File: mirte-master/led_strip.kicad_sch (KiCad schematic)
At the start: 2 parts, among them J24 led_strip

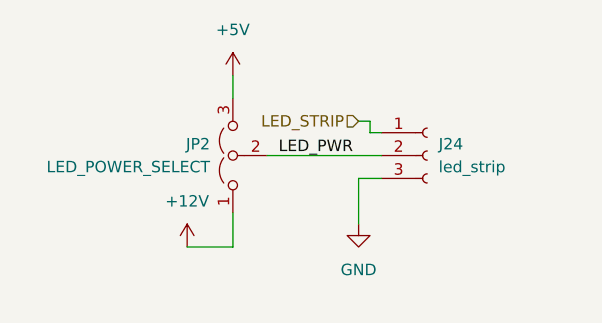
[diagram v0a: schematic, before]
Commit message: add kerco/elcos
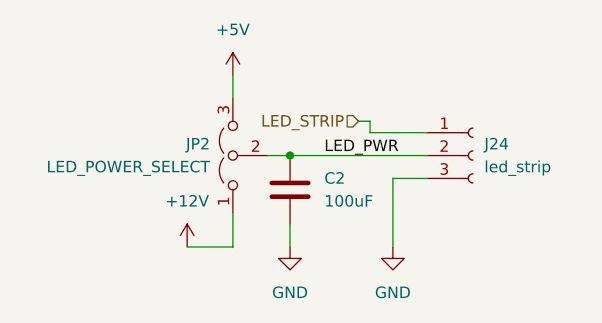
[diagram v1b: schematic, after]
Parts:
- added C2: 100uF, Capacitor_SMD:C_0805_2012Metric, symbol Device:C
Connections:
- net GND: now also C2.2
- net LED_PWR: now also C2.1
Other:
- moved on the sheet: J24
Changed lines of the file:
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@@
 (kicad_sch (version 20230121) (generator eeschema)
   (paper "A4")
-  (wire (pts (xy 113.03 73.66) (xy 110.49 73.66))
+  (junction (at 102.87 71.12) (diameter 0) (color 0 0 0 0)
+  )
+  (wire (pts (xy 118.11 73.66) (xy 114.3 73.66))
     (stroke (width 0) (type default))
   )
@@
     (stroke (width 0) (type default))
   )
-  (wire (pts (xy 111.76 68.58) (xy 113.03 68.58))
-    (stroke (width 0) (type default))
-  )
-  (wire (pts (xy 110.49 73.66) (xy 110.49 78.74))
+  (wire (pts (xy 111.76 68.58) (xy 118.11 68.58))
+    (stroke (width 0) (type default))
+  )
+  (wire (pts (xy 114.3 73.66) (xy 114.3 81.28))
     (stroke (width 0) (type default))
   )
@@
     (stroke (width 0) (type default))
   )
+  (wire (pts (xy 102.87 81.28) (xy 102.87 78.74))
+    (stroke (width 0) (type default))
+  )
   (wire (pts (xy 96.52 62.23) (xy 96.52 64.77))
     (stroke (width 0) (type default))
   )
+  (wire (pts (xy 100.33 71.12) (xy 102.87 71.12))
+    (stroke (width 0) (type default))
+  )
   (wire (pts (xy 91.44 81.28) (xy 96.52 81.28))
     (stroke (width 0) (type default))
@@
     (stroke (width 0) (type default))
   )
-  (wire (pts (xy 100.33 71.12) (xy 113.03 71.12))
-    (stroke (width 0) (type default))
-  )
-  (label "LED_PWR" (at 101.6 71.12 0) (fields_autoplaced)
+  (wire (pts (xy 102.87 71.12) (xy 118.11 71.12))
+    (stroke (width 0) (type default))
+  )
+  (label "LED_PWR" (at 106.68 71.12 0) (fields_autoplaced)
     (effects (font (size 1.27 1.27)) (justify left bottom))
   )
@@
     )
   )
+  (symbol (lib_id "Device:C") (at 102.87 74.93 0) (unit 1)
+    (in_bom yes) (on_board yes) (dnp no) (fields_autoplaced)
+    (property "Reference" "C2" (at 106.68 73.66 0)
+      (effects (font (size 1.27 1.27)) (justify left))
+    )
+    (property "Value" "100uF" (at 106.68 76.2 0)
+      (effects (font (size 1.27 1.27)) (justify left))
+    )
+    (property "Footprint" "Capacitor_SMD:C_0805_2012Metric" (at 103.8352 78.74 0)
+      (effects (font (size 1.27 1.27)) hide)
+    )
+    (property "Datasheet" "~" (at 102.87 74.93 0)
+      (effects (font (size 1.27 1.27)) hide)
+    )
+    (pin "2")
+    (pin "1")
+    (instances
+      (project "mirte-master"
+        (path "/19794465-0368-488c-958e-83b02754ebd6/17ebe4c8-09bb-4699-976c-396d27e4a3f5"
+          (reference "C2") (unit 1)
+        )
+        (path "/19794465-0368-488c-958e-83b02754ebd6/b519899b-f03f-4ac7-8598-504888127b6d"
+          (reference "C7") (unit 1)
+        )
+      )
+    )
+  )
+  (symbol (lib_id "power:GND") (at 102.87 81.28 0) (unit 1)
+    (in_bom yes) (on_board yes) (dnp no) (fields_autoplaced)
+    (property "Reference" "#PWR071" (at 102.87 87.63 0)
+      (effects (font (size 1.27 1.27)) hide)
+    )
+    (property "Value" "GND" (at 102.87 86.36 0)
+      (effects (font (size 1.27 1.27)))
+    )
+    (property "Footprint" "" (at 102.87 81.28 0)
+      (effects (font (size 1.27 1.27)) hide)
+    )
+    (property "Datasheet" "" (at 102.87 81.28 0)
+      (effects (font (size 1.27 1.27)) hide)
+    )
+    (pin "1")
+    (instances
+      (project "mirte-master"
+        (path "/19794465-0368-488c-958e-83b02754ebd6/b519899b-f03f-4ac7-8598-504888127b6d"
+          (reference "#PWR071") (unit 1)
+        )
+      )
+    )
+  )
   (symbol (lib_id "power:+12V") (at 91.44 81.28 0) (unit 1)
     (in_bom yes) (on_board yes) (dnp no) (fields_autoplaced)
@@
     )
   )
-  (symbol (lib_id "Connector:Conn_01x03_Socket") (at 118.11 71.12 0) (unit 1)
-    (in_bom yes) (on_board yes) (dnp no) (fields_autoplaced)
-    (property "Reference" "J24" (at 119.38 69.85 0)
-      (effects (font (size 1.27 1.27)) (justify left))
-    )
-    (property "Value" "led_strip" (at 119.38 72.39 0)
-      (effects (font (size 1.27 1.27)) (justify left))
-    )
-    (property "Footprint" "Connector_JST:JST_XH_B3B-XH-A_1x03_P2.50mm_Vertical" (at 118.11 71.12 0)
-      (effects (font (size 1.27 1.27)) hide)
-    )
-    (property "Datasheet" "~" (at 118.11 71.12 0)
-      (effects (font (size 1.27 1.27)) hide)
-    )
-    (property "LCSC" "C144395" (at 119.38 69.85 0)
+  (symbol (lib_id "Connector:Conn_01x03_Socket") (at 123.19 71.12 0) (unit 1)
+    (in_bom yes) (on_board yes) (dnp no)
+    (property "Reference" "J24" (at 124.46 69.85 0)
+      (effects (font (size 1.27 1.27)) (justify left))
+    )
+    (property "Value" "led_strip" (at 124.46 72.39 0)
+      (effects (font (size 1.27 1.27)) (justify left))
+    )
+    (property "Footprint" "Connector_JST:JST_XH_B3B-XH-A_1x03_P2.50mm_Vertical" (at 123.19 71.12 0)
+      (effects (font (size 1.27 1.27)) hide)
+    )
+    (property "Datasheet" "~" (at 123.19 71.12 0)
+      (effects (font (size 1.27 1.27)) hide)
+    )
+    (property "LCSC" "C144395" (at 124.46 69.85 0)
       (effects (font (size 1.27 1.27)) hide)
     )
@@
     )
   )
-  (symbol (lib_id "power:GND") (at 110.49 78.74 0) (unit 1)
-    (in_bom yes) (on_board yes) (dnp no) (fields_autoplaced)
-    (property "Reference" "#PWR055" (at 110.49 85.09 0)
-      (effects (font (size 1.27 1.27)) hide)
-    )
-    (property "Value" "GND" (at 110.49 83.82 0)
-      (effects (font (size 1.27 1.27)))
-    )
-    (property "Footprint" "" (at 110.49 78.74 0)
-      (effects (font (size 1.27 1.27)) hide)
-    )
-    (property "Datasheet" "" (at 110.49 78.74 0)
-      (effects (font (size 1.27 1.27)) hide)
-    )
+  (symbol (lib_id "power:GND") (at 114.3 81.28 0) (unit 1)
+    (in_bom yes) (on_board yes) (dnp no) (fields_autoplaced)
+    (property "Reference" "#PWR055" (at 114.3 87.63 0)
+      (effects (font (size 1.27 1.27)) hide)
+    )
+    (property "Value" "GND" (at 114.3 86.36 0)
+      (effects (font (size 1.27 1.27)))
+    )
+    (property "Footprint" "" (at 114.3 81.28 0)
+      (effects (font (size 1.27 1.27)) hide)
+    )
+    (property "Datasheet" "" (at 114.3 81.28 0)
+      (effects (font (size 1.27 1.27)) hide)
+    )

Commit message: mirte master parts jclpcb fixed
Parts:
- C2: LCSC (none) -> C15850
- J24: LCSC C144395 -> C144394
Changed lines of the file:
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@@
+      (effects (font (size 1.27 1.27)) hide)
+    )
+    (property "LCSC" "C15850" (at 102.87 74.93 0)
       (effects (font (size 1.27 1.27)) hide)
     )
@@
       (effects (font (size 1.27 1.27)) hide)
     )
-    (property "LCSC" "C144395" (at 124.46 69.85 0)
+    (property "LCSC" "C144394" (at 124.46 69.85 0)
       (effects (font (size 1.27 1.27)) hide)
     )

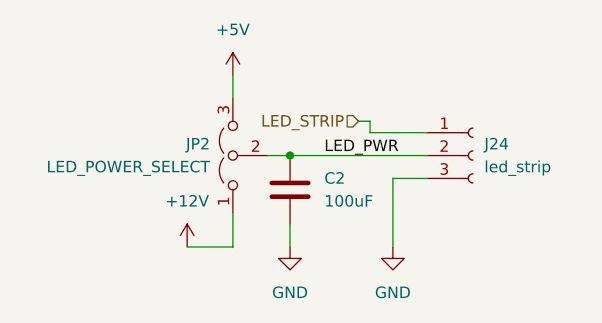
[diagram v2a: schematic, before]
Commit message: mirte-master schematic cleanup and readabilityimprovements
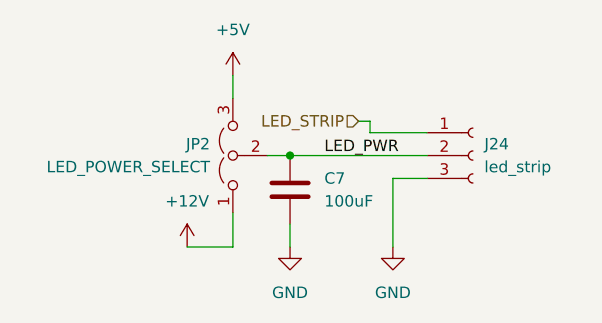
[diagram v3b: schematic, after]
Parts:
- renumbered C2 to C7
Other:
- title: (none) -> ${PROJECTNAME}
